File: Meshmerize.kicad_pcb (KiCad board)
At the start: 2 copper layers, 113.9 x 108.8 mm, 45 parts, among them M1 Motor_DC, M2 Motor_DC, SW1 SW_Push, U1 LM324, U2 ESP32-DEVKITC-32D, U3 TCRT5000, U4 TCRT5000, U5 MT3608, U6 TCRT5000, U7 TCRT5000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

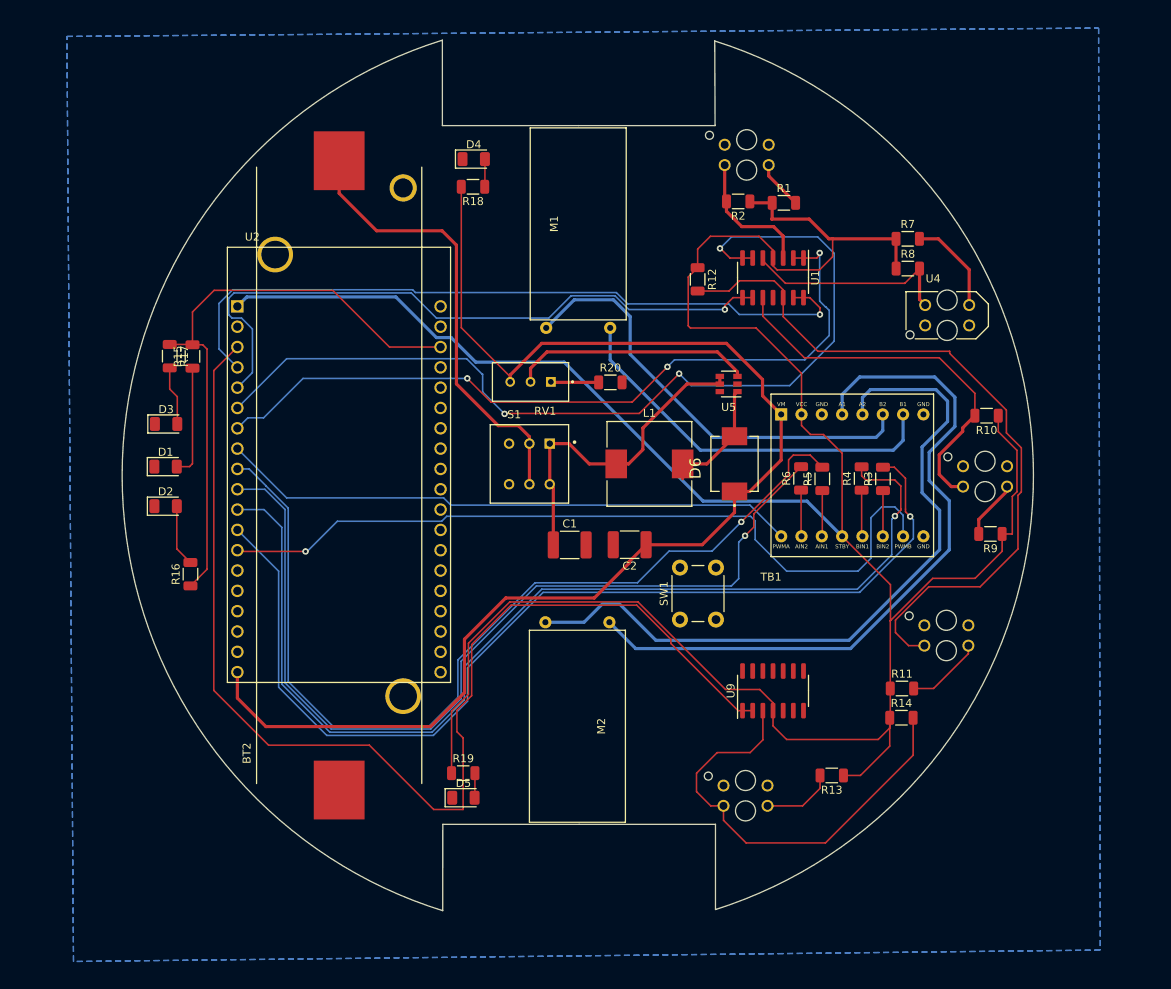
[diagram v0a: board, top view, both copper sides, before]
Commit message: Completed PCB Routing
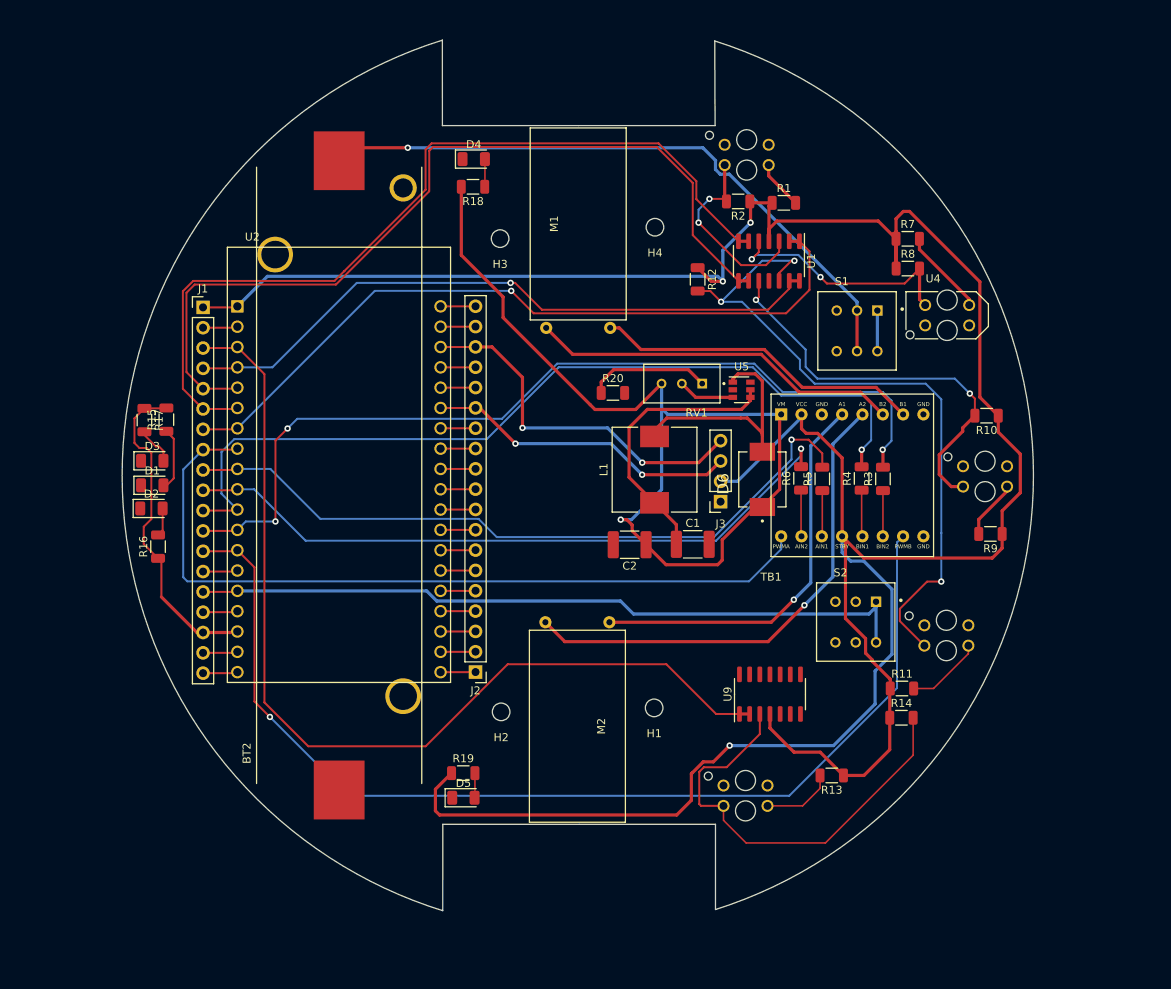
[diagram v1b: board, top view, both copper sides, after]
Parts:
- removed SW1: SW_Push, Button_Switch_THT:SW_PUSH_6mm
- added H1: MountingHole, MountingHole:MountingHole_2.2mm_M2, F.Cu at (160.6, 120.5)
- added H2: MountingHole, MountingHole:MountingHole_2.2mm_M2, F.Cu at (141.5, 121.0)
- added H3: MountingHole, MountingHole:MountingHole_2.2mm_M2, F.Cu at (141.3, 61.8)
- added H4: MountingHole, MountingHole:MountingHole_2.2mm_M2, F.Cu at (160.7, 60.4)
- added J1: Conn_01x19_Male, Connector_PinHeader_2.54mm:PinHeader_1x19_P2.54mm_Vertical, F.Cu at (104.2, 70.4)
- added J2: Conn_01x19_Male, Connector_PinHeader_2.54mm:PinHeader_1x19_P2.54mm_Vertical, F.Cu at (138.3, 116.0)
- added J3: Conn_01x04_Female, Connector_PinSocket_2.54mm:PinSocket_1x04_P2.54mm_Vertical, F.Cu at (168.9, 94.7)
- added S2: MPB04-2C33-S-D, MPB04-2C33-S-D:SW_MPB04-2C33-S-D, F.Cu at (185.8, 109.8)
- moved S1 44.2 mm to (186.0, 73.4)
- moved RV1 18.9 mm to (164.1, 80.0)
- moved C1 15.4 mm to (165.4, 100.1)
- moved R17 8.59 mm to (96.9, 84.5)
- moved R15 8.55 mm to (99.6, 84.5)
- moved R16 5.32 mm to (98.6, 100.3)
- moved D3 4.92 mm to (97.9, 89.6)
- moved D6 3.99 mm to (174.1, 91.9)
- moved D1 2.87 mm to (97.9, 92.7)
- moved U1 2.16 mm to (174.9, 64.6)
- moved D2 1.80 mm to (97.8, 95.6)
- moved U5 1.78 mm to (171.5, 80.7), turned to 0 degrees
- moved R20 1.36 mm to (155.4, 81.1)
- moved L1 0.96 mm to (160.6, 90.7), turned to 90 degrees
- moved U9 0.57 mm to (175.1, 118.8)
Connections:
- U2 pad 16: (no net) -> Net-(J1-Pad16)
- U2 pad 17: (no net) -> END_LED
- U2 pad 18: (no net) -> Net-(J1-Pad18)
- U2 pad 2: (no net) -> Net-(J1-Pad2)
- U2 pad 21: (no net) -> Net-(J2-Pad18)
- U2 pad 22: END_LED -> SDA_OLED
- U2 pad 23: (no net) -> Net-(J2-Pad16)
- U2 pad 24: (no net) -> Net-(J2-Pad15)
- U2 pad 25: (no net) -> SCL_OLED
- U2 pad 27: (no net) -> Net-(J2-Pad12)
- U2 pad 28: (no net) -> Net-(J2-Pad11)
- U2 pad 29: (no net) -> Net-(J2-Pad10)
- U2 pad 30: (no net) -> Net-(J2-Pad9)
- U2 pad 31: (no net) -> Net-(J2-Pad8)
- U2 pad 32: (no net) -> Net-(J2-Pad7)
- U2 pad 33: (no net) -> Net-(J2-Pad6)
- U2 pad 34: (no net) -> Net-(J2-Pad5)
- U2 pad 35: (no net) -> Net-(J2-Pad4)
- U2 pad 36: (no net) -> Net-(J2-Pad3)
- U2 pad 37: (no net) -> Net-(J2-Pad2)
- U2 pad 38: (no net) -> Net-(J2-Pad1)
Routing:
- net DEB: track 0.00 -> 91.5 mm
- net SDA_OLED: track 0.00 -> 45.8 mm, vias 0 -> 2
- net +V: track 165.9 -> 121.9 mm, vias 0 -> 1
- net SCL_OLED: track 0.00 -> 39.2 mm, vias 0 -> 2
- net Net-(M2-Pad2): track 89.0 -> 49.9 mm, vias 0 -> 1
- net PWMB: track 98.7 -> 134.2 mm
- net END_LED: track 74.5 -> 41.0 mm
- net A2: track 115.5 -> 85.0 mm
- net Net-(M2-Pad1): track 91.4 -> 62.1 mm, vias 0 -> 1
- net A1: track 117.6 -> 89.9 mm
- net PWMA: track 72.5 -> 99.5 mm
- net D5: track 146.1 -> 119.9 mm
- net D3: track 83.7 -> 108.7 mm, vias 1 -> 0
- net 3V3: track 342.8 -> 367.6 mm, vias 0 -> 3
- net B1: track 132.1 -> 108.4 mm
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- removed copper zone on B.Cu, net GND

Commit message: Changes made in footprint
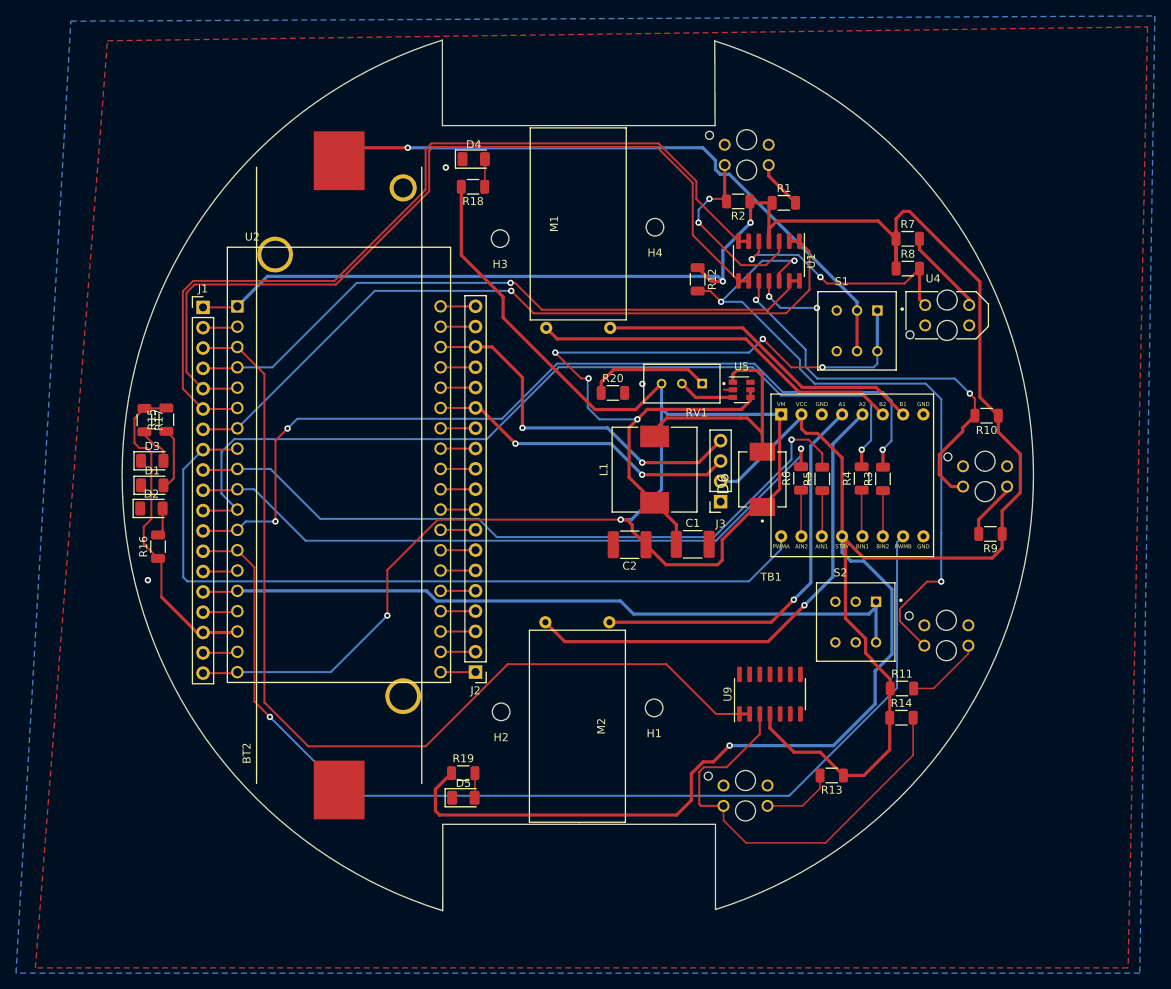
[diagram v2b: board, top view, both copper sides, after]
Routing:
- net SWO: track 40.0 -> 100.2 mm, vias 0 -> 5
- net +V: track 121.9 -> 181.0 mm, vias 1 -> 2
- net GND: track 13.1 -> 22.8 mm, vias 0 -> 5
- net Net-(D6-PadA): track 29.5 -> 30.6 mm
- added copper zone on B.Cu, net GND
- added copper zone on F.Cu, net GND
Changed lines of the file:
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@@
     (thickness 1.6)
     (drawings 11)
-    (tracks 527)
+    (tracks 560)
     (zones 0)
     (modules 52)
@@
     (pad_to_mask_clearance 0)
     (aux_axis_origin 0 0)
-    (visible_elements FFFFF77F)
+    (visible_elements FFFFFF7F)
     (pcbplotparams
       (layerselection 0x010fc_ffffffff)
@@
   (segment (start 138.251 85.5484) (end 138.2649 85.5345) (width 0.25) (layer F.Cu) (net 1) (status 30))
   (segment (start 133.89356 85.5484) (end 138.251 85.5484) (width 0.25) (layer F.Cu) (net 1) (status 30))
+  (via (at 159.1183 79.9973) (size 0.8) (drill 0.4) (layers F.Cu B.Cu) (net 1))
+  (via (at 174.9679 69.088) (size 0.8) (drill 0.4) (layers F.Cu B.Cu) (net 1))
+  (segment (start 174.9425 69.0626) (end 174.9679 69.088) (width 0.25) (layer F.Cu) (net 1))
+  (segment (start 174.9425 67.118) (end 174.9425 69.0626) (width 0.25) (layer F.Cu) (net 1))
+  (via (at 180.9369 70.4977) (size 0.8) (drill 0.4) (layers F.Cu B.Cu) (net 1))
+  (segment (start 176.3776 70.4977) (end 180.9369 70.4977) (width 0.25) (layer B.Cu) (net 1))
+  (segment (start 174.9679 69.088) (end 176.3776 70.4977) (width 0.25) (layer B.Cu) (net 1))
+  (via (at 134.5565 52.9463) (size 0.8) (drill 0.4) (layers F.Cu B.Cu) (net 1))
+  (via (at 97.3074 104.5337) (size 0.8) (drill 0.4) (layers F.Cu B.Cu) (net 1))
+  (segment (start 170.4262 80.7339) (end 169.291 80.7339) (width 0.25) (layer F.Cu) (net 1))
   (segment (start 99.2535 92.6719) (end 99.6696 92.6719) (width 0.25) (layer F.Cu) (net 2) (status 30))
   (segment (start 99.6696 92.6719) (end 100.5459 91.7956) (width 0.25) (layer F.Cu) (net 2) (status 10))
@@
   (segment (start 168.548101 66.554401) (end 169.1767 67.183) (width 0.4) (layer B.Cu) (net 7))
   (segment (start 167.7436 67.183) (end 169.1767 67.183) (width 0.4) (layer F.Cu) (net 7))
-  (segment (start 147.09698 72.99734) (end 150.40124 76.3016) (width 0.4) (layer F.Cu) (net 8))
-  (segment (start 150.40124 76.3016) (end 173.9773 76.3016) (width 0.4) (layer F.Cu) (net 8))
-  (segment (start 173.9773 76.3016) (end 178.7144 81.0387) (width 0.4) (layer F.Cu) (net 8))
   (segment (start 186.39782 81.0387) (end 189.1699 83.81078) (width 0.4) (layer F.Cu) (net 8))
   (segment (start 178.7144 81.0387) (end 186.39782 81.0387) (width 0.4) (layer F.Cu) (net 8))
-  (segment (start 155.09698 72.99734) (end 156.23314 72.99734) (width 0.4) (layer F.Cu) (net 9))
-  (segment (start 156.23314 72.99734) (end 158.93739 75.70159) (width 0.4) (layer F.Cu) (net 9))
-  (segment (start 174.36789 75.70159) (end 179.10499 80.43869) (width 0.4) (layer F.Cu) (net 9))
-  (segment (start 158.93739 75.70159) (end 174.36789 75.70159) (width 0.4) (layer F.Cu) (net 9))
+  (segment (start 172.0469 74.3712) (end 178.7144 81.0387) (width 0.4) (layer F.Cu) (net 8))
+  (segment (start 148.47084 74.3712) (end 172.0469 74.3712) (width 0.4) (layer F.Cu) (net 8))
+  (segment (start 147.09698 72.99734) (end 148.47084 74.3712) (width 0.4) (layer F.Cu) (net 8))
+  (segment (start 179.10499 80.43869) (end 188.33781 80.43869) (width 0.4) (layer F.Cu) (net 9))
+  (segment (start 171.66364 72.99734) (end 179.10499 80.43869) (width 0.4) (layer F.Cu) (net 9))
+  (segment (start 155.09698 72.99734) (end 171.66364 72.99734) (width 0.4) (layer F.Cu) (net 9))
   (segment (start 188.33781 80.43869) (end 191.7099 83.81078) (width 0.4) (layer F.Cu) (net 9))
-  (segment (start 179.10499 80.43869) (end 188.33781 80.43869) (width 0.4) (layer F.Cu) (net 9))
   (segment (start 146.99792 109.79122) (end 149.4239 112.2172) (width 0.4) (layer F.Cu) (net 10))
   (segment (start 149.4239 112.2172) (end 174.8282 112.2172) (width 0.4) (layer F.Cu) (net 10))
@@
   (segment (start 172.6262 82.0723) (end 171.5135 83.185) (width 0.4) (layer F.Cu) (net 34))
   (segment (start 171.5135 83.185) (end 159.7406 83.185) (width 0.4) (layer F.Cu) (net 34))
-  (segment (start 159.7406 83.185) (end 157.4546 85.471) (width 0.4) (layer F.Cu) (net 34))
+  (segment (start 159.7406 83.185) (end 158.50235 84.42325) (width 0.4) (layer F.Cu) (net 34))
   (segment (start 157.4546 91.6784) (end 160.6423 94.8661) (width 0.4) (layer F.Cu) (net 34))
   (segment (start 157.4546 85.471) (end 157.4546 91.6784) (width 0.4) (layer F.Cu) (net 34))
+  (segment (start 188.4934 75.9079) (end 188.4934 77.4827) (width 0.25) (layer B.Cu) (net 34))
+  (via (at 181.6227 77.9272) (size 0.8) (drill 0.4) (layers F.Cu B.Cu) (net 34))
+  (segment (start 188.0489 77.9272) (end 181.6227 77.9272) (width 0.25) (layer B.Cu) (net 34))
+  (segment (start 188.4934 77.4827) (end 188.0489 77.9272) (width 0.25) (layer B.Cu) (net 34))
+  (segment (start 158.50235 84.42325) (end 157.4546 85.471) (width 0.4) (layer F.Cu) (net 34))
+  (via (at 158.50235 84.42325) (size 0.8) (drill 0.4) (layers F.Cu B.Cu) (net 34))
+  (segment (start 158.50235 84.42325) (end 153.73985 84.42325) (width 0.25) (layer B.Cu) (net 34))
+  (segment (start 153.73985 84.42325) (end 152.2857 82.9691) (width 0.25) (layer B.Cu) (net 34))
+  (via (at 152.4 79.3115) (size 0.8) (drill 0.4) (layers F.Cu B.Cu) (net 34))
+  (segment (start 152.2857 79.4258) (end 152.4 79.3115) (width 0.25) (layer B.Cu) (net 34))
+  (segment (start 152.2857 82.9691) (end 152.2857 79.4258) (width 0.25) (layer B.Cu) (net 34))
+  (via (at 148.2344 76.0857) (size 0.8) (drill 0.4) (layers F.Cu B.Cu) (net 34))
+  (segment (start 151.4602 79.3115) (end 148.2344 76.0857) (width 0.25) (layer F.Cu) (net 34))
+  (segment (start 152.4 79.3115) (end 151.4602 79.3115) (width 0.25) (layer F.Cu) (net 34))
+  (via (at 174.174743 74.377058) (size 0.8) (drill 0.4) (layers F.Cu B.Cu) (net 34))
+  (segment (start 181.6227 77.9272) (end 177.724885 77.9272) (width 0.25) (layer F.Cu) (net 34))
+  (segment (start 177.724885 77.9272) (end 174.174743 74.377058) (width 0.25) (layer F.Cu) (net 34))
+  (segment (start 148.2344 76.0857) (end 172.466101 76.0857) (width 0.25) (layer B.Cu) (net 34))
+  (segment (start 172.466101 76.0857) (end 174.174743 74.377058) (width 0.25) (layer B.Cu) (net 34))
   (segment (start 108.36776 116.1542) (end 108.49356 116.0284) (width 0.25) (layer F.Cu) (net 35) (status 30))
   (segment (start 104.2035 116.1542) (end 108.36776 116.1542) (width 0.25) (layer F.Cu) (net 35) (status 30))
@@
   (segment (start 153.196102 83.1977) (end 158.2801 83.1977) (width 0.4) (layer F.Cu) (net 35))
   (segment (start 152.6032 82.604798) (end 153.196102 83.1977) (width 0.4) (layer F.Cu) (net 35))
+  (segment (start 108.49356 116.0284) (end 120.1662 116.0284) (width 0.25) (layer B.Cu) (net 35))
+  (via (at 127.2413 108.9533) (size 0.8) (drill 0.4) (layers F.Cu B.Cu) (net 35))
+  (segment (start 120.1662 116.0284) (end 127.2413 108.9533) (width 0.25) (layer B.Cu) (net 35))
+  (segment (start 133.542058 96.9645) (end 156.4132 96.9645) (width 0.25) (layer F.Cu) (net 35))
+  (segment (start 127.2413 103.265258) (end 133.542058 96.9645) (width 0.25) (layer F.Cu) (net 35))
+  (segment (start 127.2413 108.9533) (end 127.2413 103.265258) (width 0.25) (layer F.Cu) (net 35))
   (segment (start 160.6423 86.5661) (end 160.6423 85.7885) (width 0.4) (layer F.Cu) (net 36) (status 30))
   (segment (start 160.6423 85.7885) (end 162.1663 84.2645) (width 0.4) (layer F.Cu) (net 36) (status 10))
@@
   (segment (start 174.117 86.1441) (end 172.2374 84.2645) (width 0.4) (layer F.Cu) (net 36))
   (segment (start 162.1663 84.2645) (end 171.4119 84.2645) (width 0.4) (layer F.Cu) (net 36))
-  (segment (start 170.4262 79.7839) (end 170.4262 79.3828) (width 0.4) (layer F.Cu) (net 36))
-  (segment (start 170.4262 79.3828) (end 171.069 78.74) (width 0.4) (layer F.Cu) (net 36))
-  (segment (start 171.069 78.74) (end 173.228 78.74) (width 0.4) (layer F.Cu) (net 36))
-  (segment (start 174.117 79.629) (end 174.117 86.3854) (width 0.4) (layer F.Cu) (net 36))
-  (segment (start 173.228 78.74) (end 174.117 79.629) (width 0.4) (layer F.Cu) (net 36))
   (segment (start 174.117 86.3854) (end 174.117 86.1441) (width 0.4) (layer F.Cu) (net 36))
   (segment (start 174.117 88.4803) (end 174.117 86.3854) (width 0.4) (layer F.Cu) (net 36))
+  (segment (start 174.117 78.867) (end 174.117 86.3854) (width 0.4) (layer F.Cu) (net 36))
+  (segment (start 170.9166 78.3082) (end 173.5582 78.3082) (width 0.4) (layer F.Cu) (net 36))
+  (segment (start 170.4262 78.7986) (end 170.9166 78.3082) (width 0.4) (layer F.Cu) (net 36))
+  (segment (start 173.5582 78.3082) (end 174.117 78.867) (width 0.4) (layer F.Cu) (net 36))
+  (segment (start 170.4262 79.7839) (end 170.4262 78.7986) (width 0.4) (layer F.Cu) (net 36))
   (segment (start 153.9728 81.1276) (end 153.9728 79.7707) (width 0.4) (layer F.Cu) (net 37) (status 10))
   (segment (start 153.9728 79.7707) (end 155.5242 78.2193) (width 0.4) (layer F.Cu) (net 37))
@@
   (segment (start 138.251 72.8484) (end 138.2649 72.8345) (width 0.25) (layer F.Cu) (net 64) (status 30))
   (segment (start 133.89356 72.8484) (end 138.251 72.8484) (width 0.25) (layer F.Cu) (net 64) (status 30))
+  (zone (net 1) (net_name GND) (layer F.Cu) (hatch edge 0.508)
+    (connect_pads (clearance 0.508))
+    (min_thickness 0.254)
+    (fill yes (arc_segments 32) (thermal_gap 0.508) (thermal_bridge_width 0.508))
+    (polygon
+      (pts
+        (xy 219.837 152.9969) (xy 83.2485 152.9969) (xy 92.2528 37.1094) (xy 222.2627 35.3695)
+      )
+    )
+  )
+  (zone (net 1) (net_name GND) (layer B.Cu) (hatch edge 0.508)
+    (connect_pads yes (clearance 0.508))
+    (min_thickness 0.254)
+    (fill yes (arc_segments 32) (thermal_gap 0.508) (thermal_bridge_width 0.508))
+    (polygon
+      (pts
+        (xy 221.2975 153.6573) (xy 80.8228 153.6573) (xy 87.6808 34.6583) (xy 223.1771 34.0106)
+      )
+    )
+  )
 )
